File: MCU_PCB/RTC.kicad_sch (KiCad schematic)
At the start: 6 parts

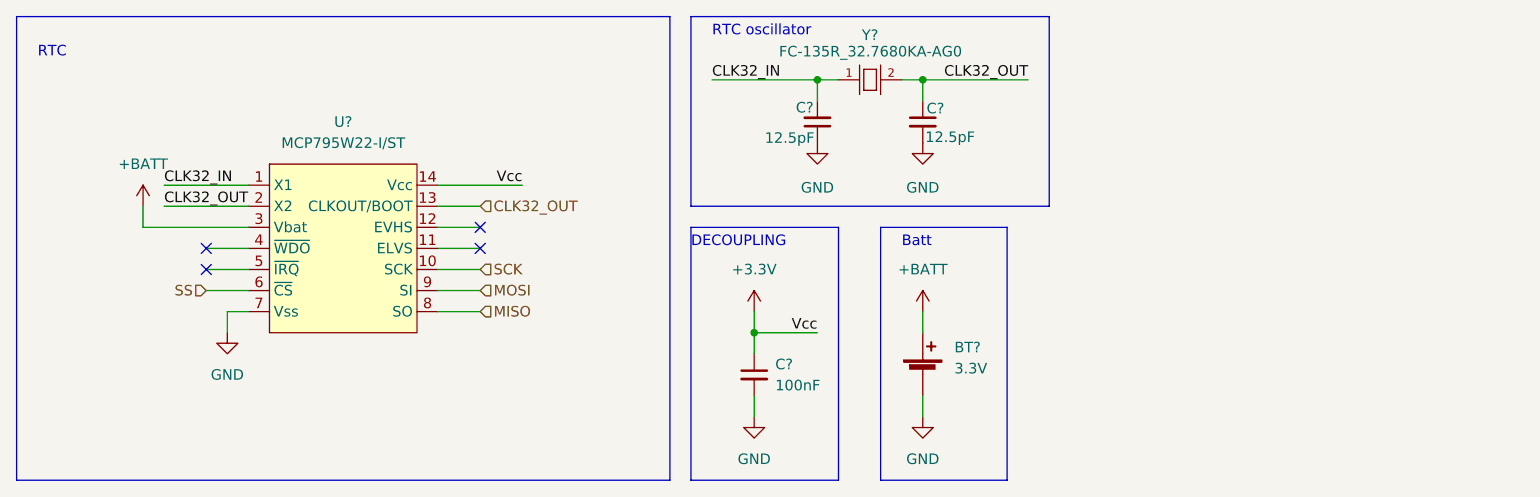
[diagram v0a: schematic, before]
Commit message: 0.1v MCU KiCad
Aesthetics needs to be improved.
Trace width needs to be changed.
More sufficient grounding.
Component placement could be changed.
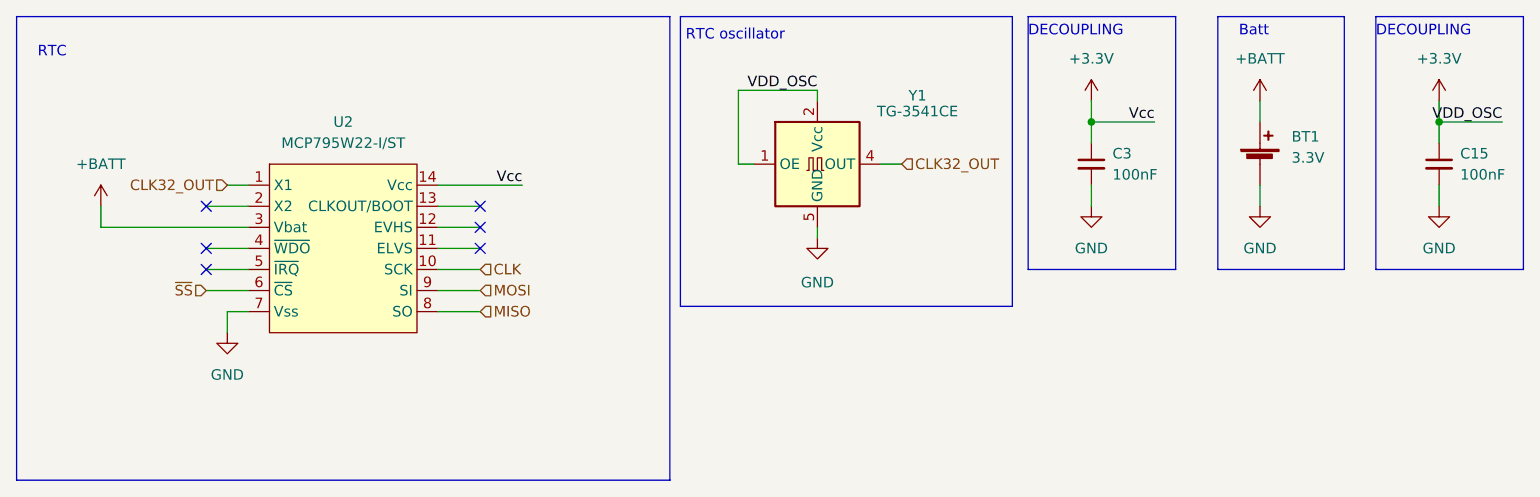
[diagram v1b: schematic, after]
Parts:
- removed C? (x2): 12.5pF, Capacitor_SMD:C_0603_1608Metric, symbol Device:C_Small
- removed Y?: FC-135R_32.7680KA-AG0, footprints:XTAL_FC-135R_32.7680KA-AG0, symbol schematics:FC-135R_32.7680KA-AG0
- added C15: 100nF, Capacitor_SMD:C_0402_1005Metric, symbol Device:C_Small
- added Y1: TG-3541CE, footprints:Oscillator_SMD_SeikoEpson_TG-3541CE_3.2x2.5mm, symbol schematics:TG-3541CE
- BT1: renamed from BT?; footprint (none) -> footprints:3034
- C3: renamed from C?; footprint (none) -> Capacitor_SMD:C_0402_1005Metric
- U2: renamed from U?; footprint (none) -> Package_SO:TSSOP-14_4.4x5mm_P0.65mm
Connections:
- net CLK32_IN is gone; now on net CLK32_OUT: U2.1 (X1)
- net +3V3: now also C15.1, Y1.1 (OE), Y1.2 (Vcc), Y1.3 (Vcc)
- net CLK32_OUT: now also Y1.4 (OUT); no longer U2.13 (CLKOUT/BOOT), U2.2 (X2)
- net GND: now also C15.2, Y1.5 (GND), Y1.7 (GND), Y1.8 (GND), Y1.9 (GND)
- net SCK renamed CLK
- net SS renamed ~{SS}
- no-connect marks 4 -> 6
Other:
- moved on the sheet: BT1, C3
